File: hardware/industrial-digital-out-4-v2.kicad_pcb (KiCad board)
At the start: 2 copper layers, 40 x 40 mm, 33 parts, among them P1 CON-SENSOR2, P2 Digital Output, P3 DEBUG, P4 BOOT, Q1 FDN5630, U1 XMC1XXX24, U2 LTV846S, U3 OPA4171AIDR, U4 DRILL, U5 DRILL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

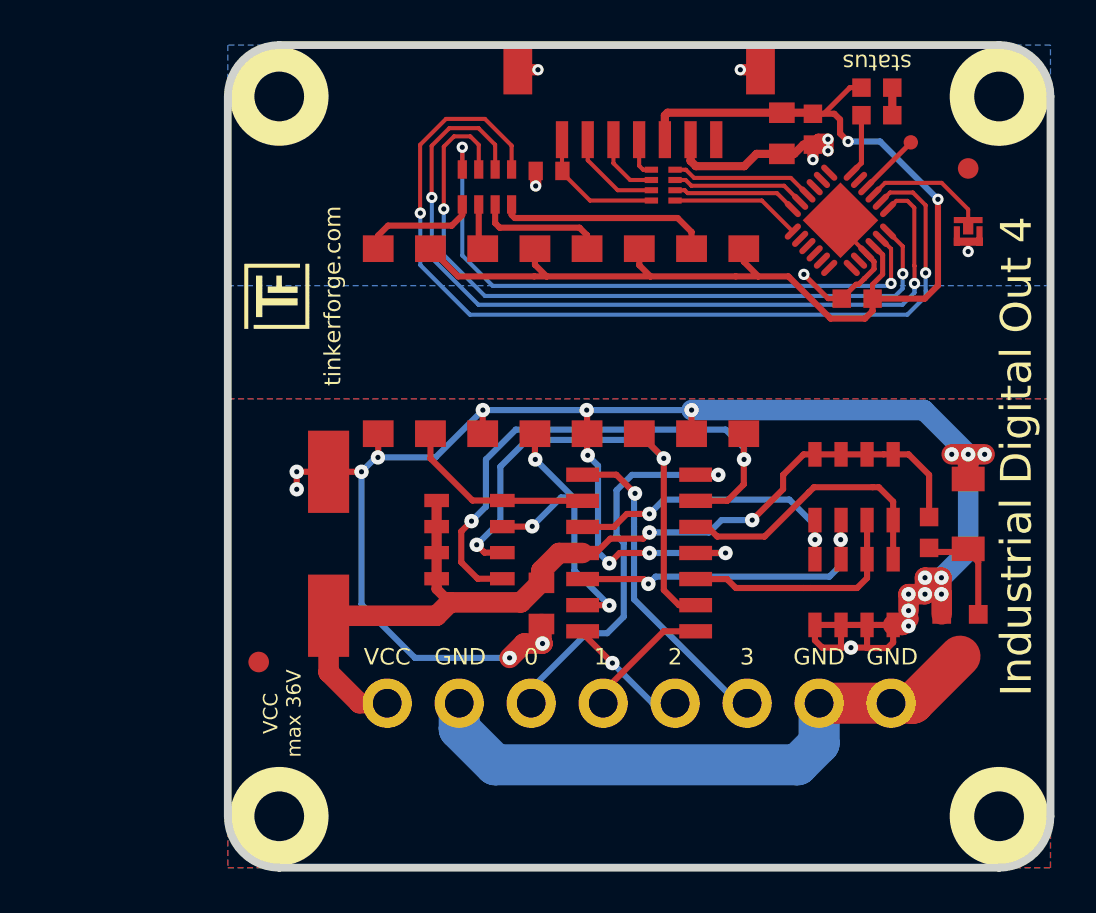
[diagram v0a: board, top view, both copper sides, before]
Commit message: Adapt routing for status leds
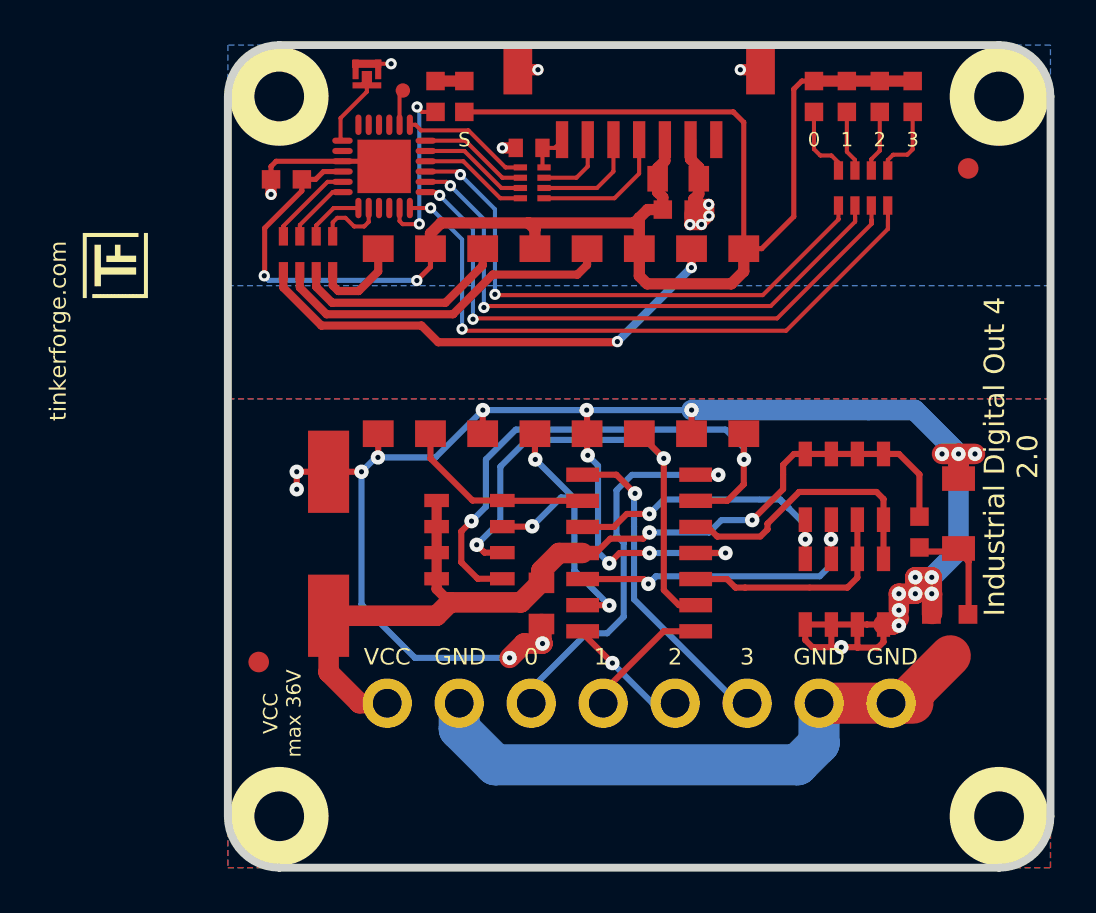
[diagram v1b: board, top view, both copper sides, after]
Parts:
- added D3: blue, D0603F, F.Cu at (126.3, 40.5)
- added D4: blue, D0603F, F.Cu at (127.9, 40.5)
- added D5: blue, D0603F, F.Cu at (129.5, 40.5)
- added D6: blue, D0603F, F.Cu at (131.1, 40.5)
- added RP6: 1k, 0603X4, F.Cu at (128.7, 45.0)
- moved G*** 53.6 mm to (161.6, 57.4)
- moved VAL 32.7 mm to (149.9, 58.6)
- moved P4 30.2 mm to (104.6, 39.5), turned to 270 degrees
- moved C6 28.3 mm to (100.7, 44.6)
- moved P3 24.8 mm to (106.3, 40.3)
- moved U1 22.3 mm to (105.4, 44.0), turned to 270 degrees
- moved R2 21.5 mm to (107.9, 40.5), turned to 90 degrees
- moved VAL 21.4 mm to (150.0, 52.2)
- moved D2 20.1 mm to (109.3, 40.5), turned to 90 degrees
- moved RP1 9.29 mm to (101.7, 48.2), turned to 180 degrees
- moved G*** 7.99 mm to (90.8, 50.4)
- moved C5 7.63 mm to (119.7, 46.0), turned to 0 degrees
- moved RP5 6.37 mm to (112.6, 44.8), turned to 90 degrees
- moved C1 5.50 mm to (119.7, 44.5), turned to 0 degrees
- moved C4 1.48 mm to (112.5, 43.0)
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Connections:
- RP1 pad 1: OUTPUT1 -> Net-(RP1-Pad1)
- RP1 pad 2: OUTPUT2 -> Net-(RP1-Pad2)
- RP1 pad 3: OUTPUT3 -> Net-(RP1-Pad3)
- RP1 pad 4: OUTPUT4 -> Net-(RP1-Pad4)
- RP1 pad 5: Net-(RP1-Pad5) -> OUTPUT1
- RP1 pad 6: Net-(RP1-Pad6) -> OUTPUT2
- RP1 pad 7: Net-(RP1-Pad7) -> OUTPUT3
- RP1 pad 8: Net-(RP1-Pad8) -> OUTPUT4
- U1 pad 15: Net-(P4-Pad2) -> Net-(U1-Pad15)
- U1 pad 16: Net-(P3-Pad1) -> Net-(U1-Pad16)
- U1 pad 17: Net-(U1-Pad17) -> Net-(R2-Pad1)
- U1 pad 18: Net-(R2-Pad1) -> Net-(RP6-Pad4)
- U1 pad 2: Net-(U1-Pad2) -> Net-(P3-Pad1)
- U1 pad 7: Net-(U1-Pad7) -> Net-(P4-Pad2)
- U2 pad 2: Net-(RP1-Pad8) -> Net-(RP1-Pad1)
- U2 pad 4: Net-(RP1-Pad7) -> Net-(RP1-Pad2)
- U2 pad 6: Net-(RP1-Pad6) -> Net-(RP1-Pad3)
- U2 pad 8: Net-(RP1-Pad5) -> Net-(RP1-Pad4)
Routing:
- net OUTPUT1: track 45.5 -> 3.46 mm, vias 2 -> 0
- net OUTPUT2: track 40.8 -> 2.93 mm, vias 2 -> 0
- net Net-(RP6-Pad4): track 0.00 -> 31.9 mm, vias 0 -> 2
- net OUTPUT3: track 34.9 -> 3.29 mm, vias 2 -> 0
- net Net-(RP6-Pad3): track 0.00 -> 29.9 mm, vias 0 -> 2
- net Net-(RP6-Pad2): track 0.00 -> 28.8 mm, vias 0 -> 2
- net Net-(RP6-Pad1): track 0.00 -> 27.2 mm, vias 0 -> 2
- net OUTPUT4: track 30.2 -> 4.71 mm, vias 2 -> 0
- net Net-(RP1-Pad1): track 0.00 -> 24.2 mm, vias 0 -> 2
- net 3V3: track 58.6 -> 79.0 mm
- net Net-(RP1-Pad2): track 0.00 -> 17.1 mm
- net Net-(RP1-Pad3): track 0.00 -> 11.4 mm
- net Net-(RP1-Pad8): track 10.4 -> 0.00 mm
- net Net-(RP1-Pad7): track 6.27 -> 0.00 mm
- net Net-(RP1-Pad5): track 5.66 -> 0.00 mm
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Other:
- board text added: "Industrial Digital Out 4 2.0"
- board text added: "S"
- board text removed: "Industrial Digital Out 4"
- board text removed: "ToDo: Massefläche oben hier wichtig?"
- board text removed: "status"

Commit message: Change routing
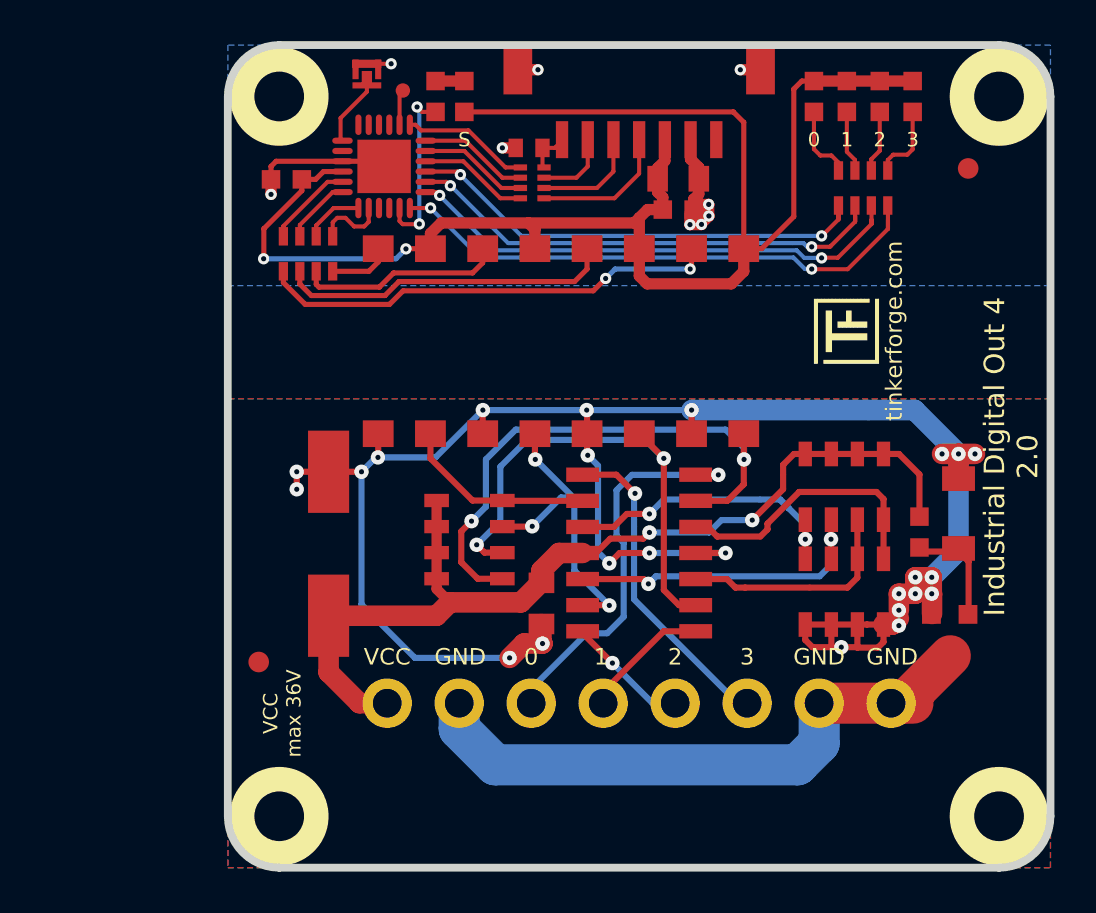
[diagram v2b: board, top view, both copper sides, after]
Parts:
- moved VAL 42.1 mm to (107.8, 58.0), turned to 90 degrees
- moved G*** 35.7 mm to (126.3, 53.5)
- moved G*** 33.8 mm to (127.8, 58.0), turned to 90 degrees
- moved VAL 32.8 mm to (117.7, 58.1), turned to 90 degrees
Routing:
- net Net-(RP6-Pad3): track 29.9 -> 24.8 mm
- net Net-(RP6-Pad4): track 31.9 -> 26.9 mm
- net Net-(RP6-Pad2): track 28.8 -> 24.5 mm
- net Net-(RP6-Pad1): track 27.2 -> 23.1 mm
- net 3V3: track 79.0 -> 77.2 mm
- net Net-(RP1-Pad1): track 24.2 -> 22.5 mm
- net Net-(RP1-Pad4): track 4.52 -> 3.05 mm
- net Net-(RP1-Pad3): track 11.4 -> 10.6 mm
- net Net-(RP1-Pad2): track 17.1 -> 16.3 mm
